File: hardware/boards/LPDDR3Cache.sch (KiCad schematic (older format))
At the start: 2 parts, among them U1 ECP5UM5G-381caBGA, U4 IS43TR16256B-125KBL

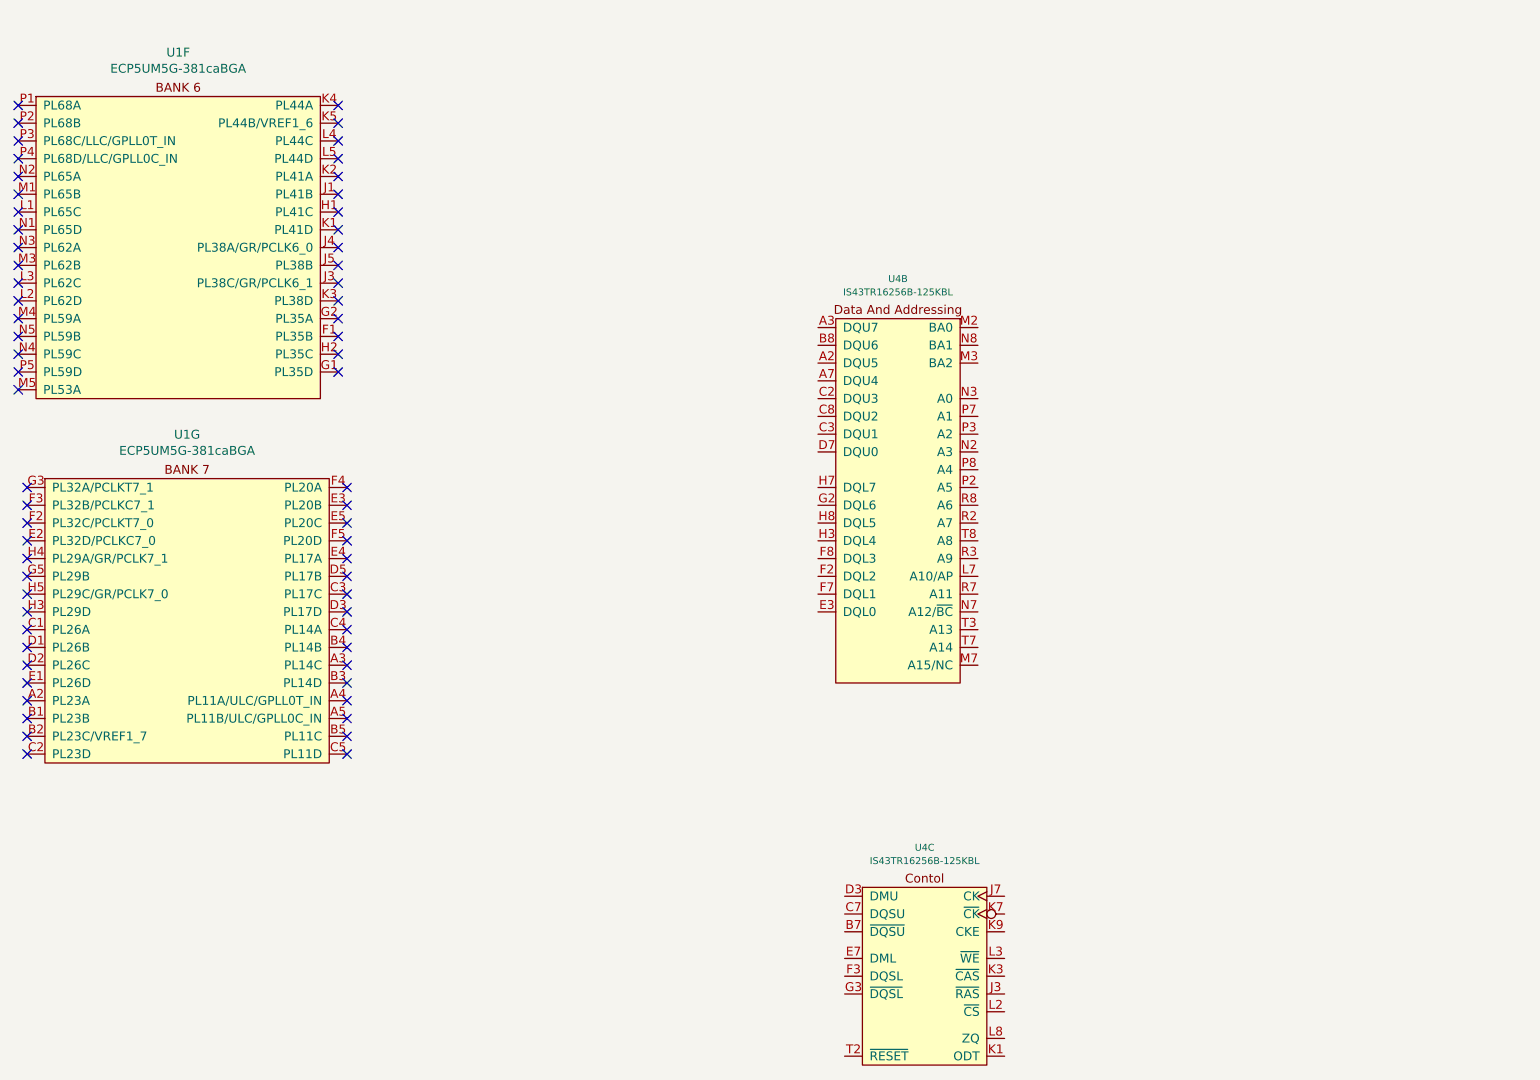
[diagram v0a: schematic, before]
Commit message: Added the data and address buses for the DDR
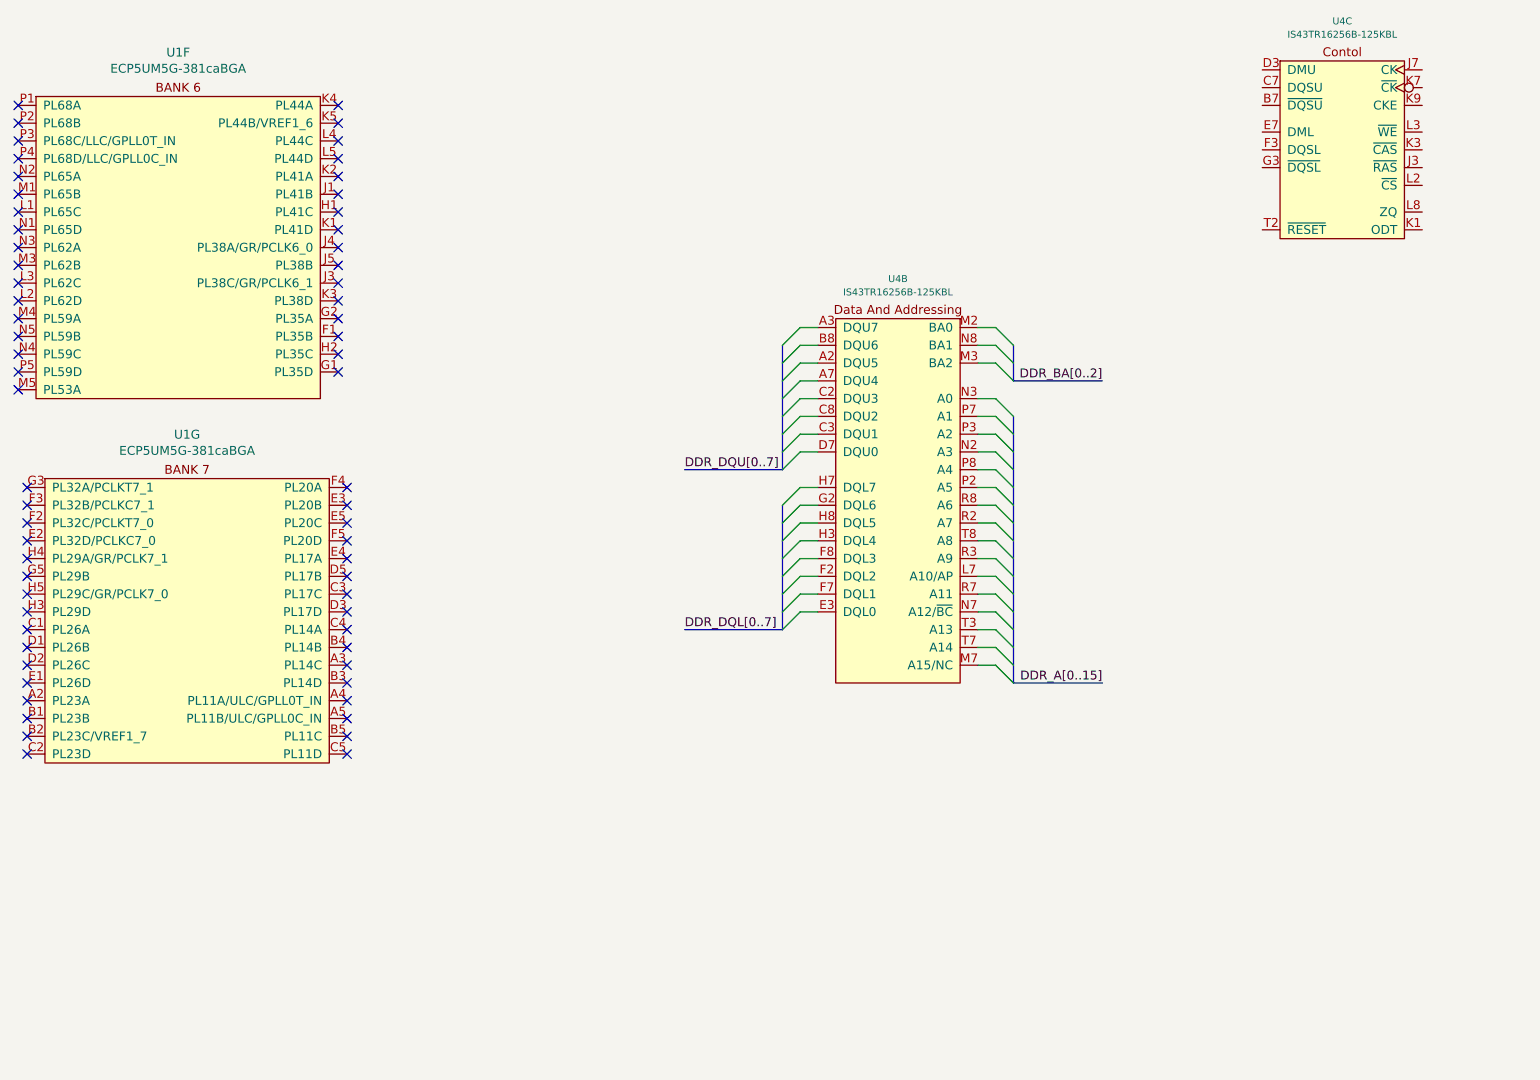
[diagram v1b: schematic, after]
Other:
- moved on the sheet: U4C
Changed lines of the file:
@@
 L lethalbit-memory:IS43TR16256B-125KBL U4
 U 3 1 5F1E0638
-P 10050 6400
-F 0 "U4" H 10050 6874 39  0000 C CNN
-F 1 "IS43TR16256B-125KBL" H 10050 6799 39  0000 C CNN
-F 2 "Package_BGA:BGA-96_9.0x13.0mm_Layout2x3x16_P0.8mm" H 10050 6800 39  0001 C CNN
-F 3 "http://www.issi.com/WW/pdf/43-46TR16256B-85120BL.pdf" H 10050 6800 39  0001 C CNN
-F 4 "ISSI" H 10050 6400 50  0001 C CNN "MFR"
-F 5 "IS43TR16256B-125KBL" H 10050 6400 50  0001 C CNN "MPN"
-	3    10050 6400
+P 12400 1750
+F 0 "U4" H 12400 2224 39  0000 C CNN
+F 1 "IS43TR16256B-125KBL" H 12400 2149 39  0000 C CNN
+F 2 "Package_BGA:BGA-96_9.0x13.0mm_Layout2x3x16_P0.8mm" H 12400 2150 39  0001 C CNN
+F 3 "http://www.issi.com/WW/pdf/43-46TR16256B-85120BL.pdf" H 12400 2150 39  0001 C CNN
+F 4 "ISSI" H 12400 1750 50  0001 C CNN "MFR"
+F 5 "IS43TR16256B-125KBL" H 12400 1750 50  0001 C CNN "MPN"
+	3    12400 1750
 	1    0    0    -1
 $EndComp
+Entry Wire Line
+	10450 3000 10550 3100
+Entry Wire Line
+	10450 3100 10550 3200
+Entry Wire Line
+	10450 3200 10550 3300
+Entry Wire Line
+	10450 3400 10550 3500
+Entry Wire Line
+	10450 3500 10550 3600
+Entry Wire Line
+	10450 3600 10550 3700
+Entry Wire Line
+	10450 3700 10550 3800
+Entry Wire Line
+	10450 3800 10550 3900
+Entry Wire Line
+	10450 3900 10550 4000
+Entry Wire Line
+	10450 4000 10550 4100
+Entry Wire Line
+	10450 4100 10550 4200
+Entry Wire Line
+	10450 4200 10550 4300
+Entry Wire Line
+	10450 4300 10550 4400
+Entry Wire Line
+	10450 4400 10550 4500
+Entry Wire Line
+	10450 4500 10550 4600
+Entry Wire Line
+	10450 4600 10550 4700
+Entry Wire Line
+	10450 4700 10550 4800
+Entry Wire Line
+	10450 4800 10550 4900
+Entry Wire Line
+	10450 4900 10550 5000
+Entry Wire Line
+	9250 3100 9350 3000
+Entry Wire Line
+	9250 3200 9350 3100
+Entry Wire Line
+	9250 3300 9350 3200
+Entry Wire Line
+	9250 3400 9350 3300
+Entry Wire Line
+	9250 3500 9350 3400
+Entry Wire Line
+	9250 3600 9350 3500
+Entry Wire Line
+	9250 3700 9350 3600
+Entry Wire Line
+	9250 3800 9350 3700
+Entry Wire Line
+	9250 4000 9350 3900
+Entry Wire Line
+	9250 4100 9350 4000
+Entry Wire Line
+	9250 4200 9350 4100
+Entry Wire Line
+	9250 4300 9350 4200
+Entry Wire Line
+	9250 4400 9350 4300
+Entry Wire Line
+	9250 4500 9350 4400
+Entry Wire Line
+	9250 4600 9350 4500
+Entry Wire Line
+	9250 4700 9350 4600
+Wire Wire Line
+	9450 3000 9350 3000
+Wire Wire Line
+	9450 3100 9350 3100
+Wire Wire Line
+	9450 3200 9350 3200
+Wire Wire Line
+	9450 3300 9350 3300
+Wire Wire Line
+	9450 3400 9350 3400
+Wire Wire Line
+	9450 3500 9350 3500
+Wire Wire Line
+	9450 3600 9350 3600
+Wire Wire Line
+	9450 3700 9350 3700
+Wire Wire Line
+	9450 3900 9350 3900
+Wire Wire Line
+	9450 4000 9350 4000
+Wire Wire Line
+	9450 4100 9350 4100
+Wire Wire Line
+	9450 4200 9350 4200
+Wire Wire Line
+	9450 4300 9350 4300
+Wire Wire Line
+	9450 4400 9350 4400
+Wire Wire Line
+	9350 4500 9450 4500
+Wire Wire Line
+	9350 4600 9450 4600
+Wire Wire Line
+	10350 4900 10450 4900
+Wire Wire Line
+	10350 4800 10450 4800
+Wire Wire Line
+	10350 4700 10450 4700
+Wire Wire Line
+	10350 4600 10450 4600
+Wire Wire Line
+	10350 4500 10450 4500
+Wire Wire Line
+	10350 4400 10450 4400
+Wire Wire Line
+	10350 4300 10450 4300
+Wire Wire Line
+	10350 4200 10450 4200
+Wire Wire Line
+	10350 4100 10450 4100
+Wire Wire Line
+	10350 4000 10450 4000
+Wire Wire Line
+	10350 3900 10450 3900
+Wire Wire Line
+	10350 3800 10450 3800
+Wire Wire Line
+	10350 3700 10450 3700
+Wire Wire Line
+	10350 3600 10450 3600
+Wire Wire Line
+	10350 3400 10450 3400
+Wire Wire Line
+	10350 3500 10450 3500
+Wire Wire Line
+	10350 3000 10450 3000
+Wire Wire Line
+	10350 3100 10450 3100
+Wire Wire Line
+	10350 3200 10450 3200
+Wire Bus Line
+	10550 3300 11050 3300
+Wire Bus Line
+	10550 5000 11050 5000
+Wire Bus Line
+	9250 4700 8700 4700
+Wire Bus Line
+	9250 3800 8700 3800
+Text Label 11050 3300 2    50   ~ 0
+DDR_BA[0..2]
+Text Label 11050 5000 2    50   ~ 0
+DDR_A[0..15]
+Text Label 8700 4700 0    50   ~ 0
+DDR_DQL[0..7]
+Wire Bus Line
+	10550 3100 10550 3300
+Wire Bus Line
+	9250 3100 9250 3800
+Wire Bus Line
+	9250 4000 9250 4700
+Wire Bus Line
+	10550 3500 10550 5000
+Text Label 8700 3800 0    50   ~ 0
+DDR_DQU[0..7]
 $EndSCHEMATC

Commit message: Worked on a bit of the power side for the DDR3 Cache
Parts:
- added R37: 240, Resistor_SMD:R_0603_1608Metric, symbol Device:R_Small
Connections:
- net at U4.L8 (ZQ): now also R37.1
- new net GND: R37.2
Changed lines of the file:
@@
 Text Label 8700 4700 0    50   ~ 0
 DDR_DQL[0..7]
+Text Label 8700 3800 0    50   ~ 0
+DDR_DQU[0..7]
+$Comp
+L Device:R_Small R37
+U 1 1 5FB43313
+P 13200 2500
+F 0 "R37" H 13259 2546 50  0000 L CNN
+F 1 "240" H 13259 2455 50  0000 L CNN
+F 2 "Resistor_SMD:R_0603_1608Metric" H 13200 2500 50  0001 C CNN
+F 3 "~" H 13200 2500 50  0001 C CNN
+F 4 "Stackepole Electronics Inc." H 13200 2500 50  0001 C CNN "MFR"
+F 5 "RNCF0603TKY250R" H 13200 2500 50  0001 C CNN "MPN"
+	1    13200 2500
+	1    0    0    -1
+$EndComp
+$Comp
+L power:GND #PWR0123
+U 1 1 5FB44F99
+P 13200 2700
+F 0 "#PWR0123" H 13200 2450 50  0001 C CNN
+F 1 "GND" H 13205 2527 50  0000 C CNN
+F 2 "" H 13200 2700 50  0001 C CNN
+F 3 "" H 13200 2700 50  0001 C CNN
+	1    13200 2700
+	1    0    0    -1
+$EndComp
+Wire Wire Line
+	13200 2600 13200 2700
+Wire Wire Line
+	13200 2400 13200 2350
+Wire Wire Line
+	13200 2350 12850 2350
 Wire Bus Line
 	10550 3100 10550 3300
@@
 Wire Bus Line
 	10550 3500 10550 5000
-Text Label 8700 3800 0    50   ~ 0
-DDR_DQU[0..7]
 $EndSCHEMATC
